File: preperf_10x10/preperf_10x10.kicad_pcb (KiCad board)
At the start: 2 copper layers, 355.3 x 107.6 mm, 1356 parts, among them J1 Conn_01x02_Pin, J2 Conn_01x02_Pin, J3 Conn_01x02_Pin, J4 Conn_01x01_Pin, J5 Conn_01x01_Pin, J6 Conn_01x01_Pin, J7 Conn_01x01_Pin, J8 Conn_01x01_Pin, J9 Conn_01x01_Pin, Q1 BC548, Q2 BC558, SW1 SW_DIP_x06, SW2 SW_Push, U1 LM7805_TO220, U10 74LS14, U2 74LS08, U3 74LS32, U4 74LS04, U5 74LS02, U6 7400, U7 74LS86

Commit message: Update. Delete TP4
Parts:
- removed 2 (x1296): , 
- removed the REF** at (451.5, 55.9)
- removed the REF** at (451.5, 150.5)
- removed the REF** at (356.9, 55.9)
- removed the REF** at (356.9, 150.5)
- RN1: footprint Resistor_THT:R_Array_SIP7 -> Resistor_THT:R_Array_SIP8
- moved D4 2.54 mm to (147.3, 66.0)
- moved D6 2.54 mm to (147.3, 71.1)
- moved D8 2.54 mm to (147.3, 76.2)
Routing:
- net GND: track 385.8 -> 360.4 mm, vias 4 -> 6
- net +5V: track 335.1 -> 330.0 mm, vias 9 -> 11
- net /Logica/E: track 61.0 -> 63.5 mm
- net /Logica/C: track 50.8 -> 53.3 mm
- net /Logica/A: track 12.7 -> 15.2 mm
- net Net-(D8-A): track 7.62 -> 5.08 mm
- net Net-(D6-A): track 7.62 -> 5.08 mm
- net Net-(D4-A): track 7.62 -> 5.08 mm
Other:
- board size 355.3 x 107.6 mm -> 100 x 100 mm

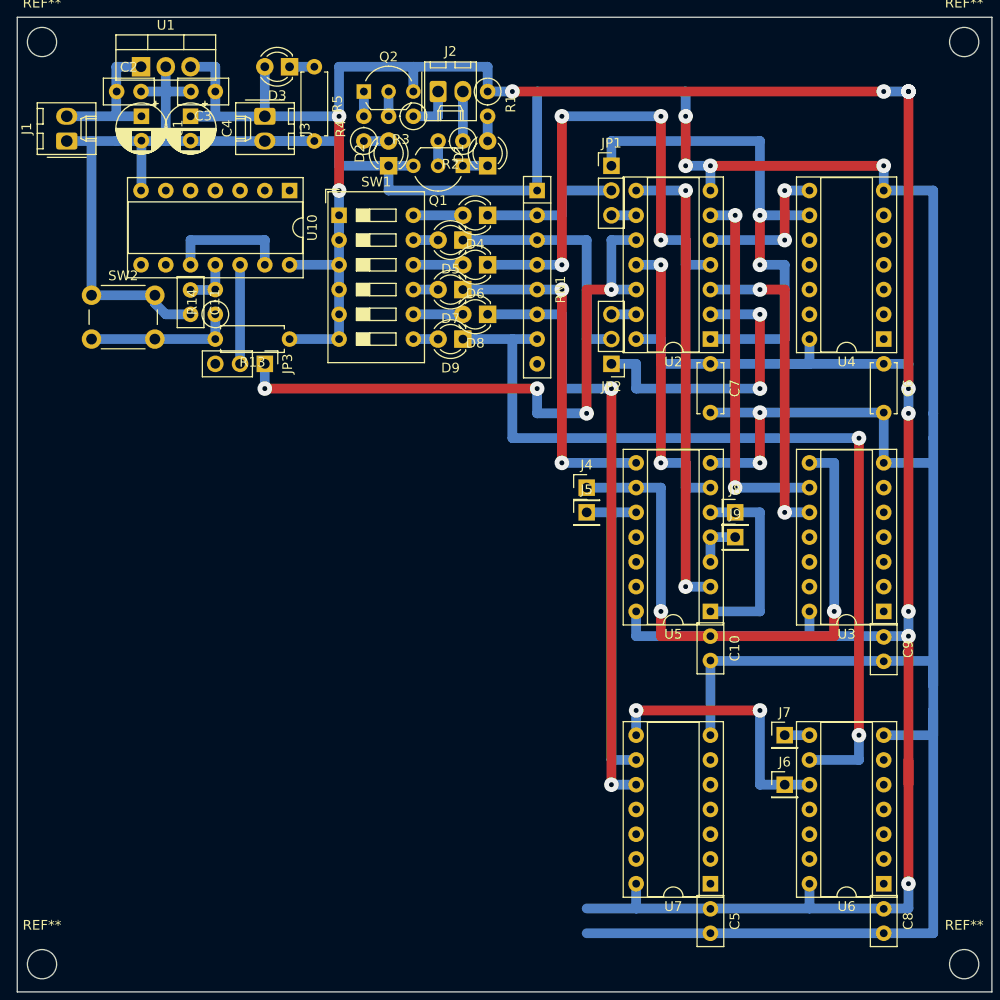
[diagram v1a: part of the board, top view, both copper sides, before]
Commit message: Added BCD Up counter with JK FF
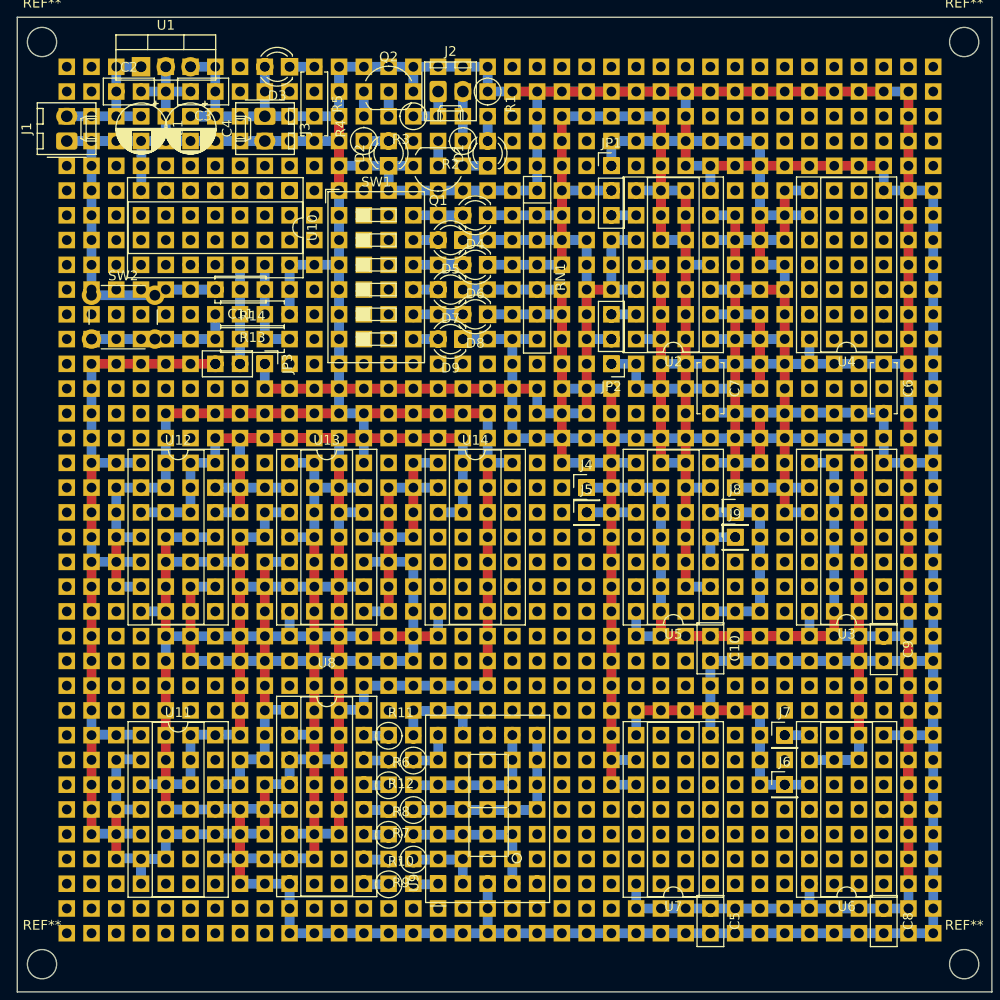
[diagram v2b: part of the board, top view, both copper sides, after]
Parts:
- added 1: , , F.Cu at (106.7, 50.8)
- added 10: , , F.Cu at (129.5, 50.8)
- added 100: , , F.Cu at (175.3, 55.9)
- added 1000: , , F.Cu at (175.3, 119.4)
- added 1001: , , F.Cu at (177.8, 119.4)
- added 1002: , , F.Cu at (180.3, 119.4)
- added 1003: , , F.Cu at (182.9, 119.4)
- added 1004: , , F.Cu at (185.4, 119.4)
- added 1005: , , F.Cu at (188.0, 119.4)
- added 1006: , , F.Cu at (190.5, 119.4)
- added 1007: , , F.Cu at (193.0, 119.4)
- added 1008: , , F.Cu at (104.1, 121.9)
- added 1009: , , F.Cu at (106.7, 121.9)
- added 101: , , F.Cu at (177.8, 55.9)
- added 1010: , , F.Cu at (109.2, 121.9)
- added 1011: , , F.Cu at (111.8, 121.9)
- added 1012: , , F.Cu at (114.3, 121.9)
- added 1013: , , F.Cu at (116.8, 121.9)
- added 1014: , , F.Cu at (119.4, 121.9)
- added 1015: , , F.Cu at (121.9, 121.9)
- added 1016: , , F.Cu at (124.5, 121.9)
- added 1017: , , F.Cu at (127.0, 121.9)
- added 1018: , , F.Cu at (129.5, 121.9)
- added 1019: , , F.Cu at (132.1, 121.9)
- added 102: , , F.Cu at (180.3, 55.9)
- added 1020: , , F.Cu at (134.6, 121.9)
- added 1021: , , F.Cu at (137.2, 121.9)
- added 1022: , , F.Cu at (139.7, 121.9)
- added 1023: , , F.Cu at (142.2, 121.9)
- added 1024: , , F.Cu at (144.8, 121.9)
- added 1025: , , F.Cu at (147.3, 121.9)
- added 1026: , , F.Cu at (149.9, 121.9)
- added 1027: , , F.Cu at (152.4, 121.9)
- added 1028: , , F.Cu at (154.9, 121.9)
- added 1029: , , F.Cu at (157.5, 121.9)
- added 103: , , F.Cu at (182.9, 55.9)
- added 1030: , , F.Cu at (160.0, 121.9)
- added 1031: , , F.Cu at (162.6, 121.9)
- added 1032: , , F.Cu at (165.1, 121.9)
- added 1033: , , F.Cu at (167.6, 121.9)
- added 1034: , , F.Cu at (170.2, 121.9)
- added 1035: , , F.Cu at (172.7, 121.9)
- added 1036: , , F.Cu at (175.3, 121.9)
- added 1037: , , F.Cu at (177.8, 121.9)
- added 1038: , , F.Cu at (180.3, 121.9)
- added 1039: , , F.Cu at (182.9, 121.9)
- added 104: , , F.Cu at (185.4, 55.9)
- added 1040: , , F.Cu at (185.4, 121.9)
- added 1041: , , F.Cu at (188.0, 121.9)
- added 1042: , , F.Cu at (190.5, 121.9)
- added 1043: , , F.Cu at (193.0, 121.9)
- added 1044: , , F.Cu at (104.1, 124.5)
- added 1045: , , F.Cu at (106.7, 124.5)
- added 1046: , , F.Cu at (109.2, 124.5)
- added 1047: , , F.Cu at (111.8, 124.5)
- added 1048: , , F.Cu at (114.3, 124.5)
- added 1049: , , F.Cu at (116.8, 124.5)
- added 105: , , F.Cu at (188.0, 55.9)
- added 1050: , , F.Cu at (119.4, 124.5)
- added 1051: , , F.Cu at (121.9, 124.5)
- added 1052: , , F.Cu at (124.5, 124.5)
- added 1053: , , F.Cu at (127.0, 124.5)
- added 1054: , , F.Cu at (129.5, 124.5)
- added 1055: , , F.Cu at (132.1, 124.5)
- added 1056: , , F.Cu at (134.6, 124.5)
- added 1057: , , F.Cu at (137.2, 124.5)
- added 1058: , , F.Cu at (139.7, 124.5)
- added 1059: , , F.Cu at (142.2, 124.5)
- added 106: , , F.Cu at (190.5, 55.9)
- added 1060: , , F.Cu at (144.8, 124.5)
- added 1061: , , F.Cu at (147.3, 124.5)
- added 1062: , , F.Cu at (149.9, 124.5)
- added 1063: , , F.Cu at (152.4, 124.5)
- added 1064: , , F.Cu at (154.9, 124.5)
- added 1065: , , F.Cu at (157.5, 124.5)
- added 1066: , , F.Cu at (160.0, 124.5)
- added 1067: , , F.Cu at (162.6, 124.5)
- added 1068: , , F.Cu at (165.1, 124.5)
- added 1069: , , F.Cu at (167.6, 124.5)
- added 107: , , F.Cu at (193.0, 55.9)
- added 1070: , , F.Cu at (170.2, 124.5)
- added 1071: , , F.Cu at (172.7, 124.5)
- added 1072: , , F.Cu at (175.3, 124.5)
- added 1073: , , F.Cu at (177.8, 124.5)
- added 1074: , , F.Cu at (180.3, 124.5)
- added 1075: , , F.Cu at (182.9, 124.5)
- added 1076: , , F.Cu at (185.4, 124.5)
- added 1077: , , F.Cu at (188.0, 124.5)
- added 1078: , , F.Cu at (190.5, 124.5)
- added 1079: , , F.Cu at (193.0, 124.5)
- added 108: , , F.Cu at (104.1, 58.4)
- added 1080: , , F.Cu at (104.1, 127.0)
- added 1081: , , F.Cu at (106.7, 127.0)
- added 1082: , , F.Cu at (109.2, 127.0)
- added 1083: , , F.Cu at (111.8, 127.0)
- added 1084: , , F.Cu at (114.3, 127.0)
- added 1085: , , F.Cu at (116.8, 127.0)
- added 1086: , , F.Cu at (119.4, 127.0)
- added 1087: , , F.Cu at (121.9, 127.0)
- added 1088: , , F.Cu at (124.5, 127.0)
- added 1089: , , F.Cu at (127.0, 127.0)
- added 109: , , F.Cu at (106.7, 58.4)
- added 1090: , , F.Cu at (129.5, 127.0)
- added 1091: , , F.Cu at (132.1, 127.0)
- added 1092: , , F.Cu at (134.6, 127.0)
- added 1093: , , F.Cu at (137.2, 127.0)
- added 1094: , , F.Cu at (139.7, 127.0)
- added 1095: , , F.Cu at (142.2, 127.0)
- added 1096: , , F.Cu at (144.8, 127.0)
- added 1097: , , F.Cu at (147.3, 127.0)
- added 1098: , , F.Cu at (149.9, 127.0)
- added 1099: , , F.Cu at (152.4, 127.0)
- added 11: , , F.Cu at (132.1, 50.8)
- added 110: , , F.Cu at (109.2, 58.4)
- added 1100: , , F.Cu at (154.9, 127.0)
- added 1101: , , F.Cu at (157.5, 127.0)
- added 1102: , , F.Cu at (160.0, 127.0)
- added 1103: , , F.Cu at (162.6, 127.0)
- added 1104: , , F.Cu at (165.1, 127.0)
- added 1105: , , F.Cu at (167.6, 127.0)
- added 1106: , , F.Cu at (170.2, 127.0)
- added 1107: , , F.Cu at (172.7, 127.0)
- added 1108: , , F.Cu at (175.3, 127.0)
- added 1109: , , F.Cu at (177.8, 127.0)
- added 111: , , F.Cu at (111.8, 58.4)
- added 1110: , , F.Cu at (180.3, 127.0)
- added 1111: , , F.Cu at (182.9, 127.0)
- added 1112: , , F.Cu at (185.4, 127.0)
- added 1113: , , F.Cu at (188.0, 127.0)
- added 1114: , , F.Cu at (190.5, 127.0)
- added 1115: , , F.Cu at (193.0, 127.0)
- added 1116: , , F.Cu at (104.1, 129.5)
- added 1117: , , F.Cu at (106.7, 129.5)
- added 1118: , , F.Cu at (109.2, 129.5)
- added 1119: , , F.Cu at (111.8, 129.5)
- added 112: , , F.Cu at (114.3, 58.4)
- added 1120: , , F.Cu at (114.3, 129.5)
- added 1121: , , F.Cu at (116.8, 129.5)
- added 1122: , , F.Cu at (119.4, 129.5)
- added 1123: , , F.Cu at (121.9, 129.5)
- added 1124: , , F.Cu at (124.5, 129.5)
- added 1125: , , F.Cu at (127.0, 129.5)
- added 1126: , , F.Cu at (129.5, 129.5)
- added 1127: , , F.Cu at (132.1, 129.5)
- added 1128: , , F.Cu at (134.6, 129.5)
- added 1129: , , F.Cu at (137.2, 129.5)
- added 113: , , F.Cu at (116.8, 58.4)
- added 1130: , , F.Cu at (139.7, 129.5)
- added 1131: , , F.Cu at (142.2, 129.5)
- added 1132: , , F.Cu at (144.8, 129.5)
- added 1133: , , F.Cu at (147.3, 129.5)
- added 1134: , , F.Cu at (149.9, 129.5)
- added 1135: , , F.Cu at (152.4, 129.5)
- added 1136: , , F.Cu at (154.9, 129.5)
- added 1137: , , F.Cu at (157.5, 129.5)
- added 1138: , , F.Cu at (160.0, 129.5)
- added 1139: , , F.Cu at (162.6, 129.5)
- added 114: , , F.Cu at (119.4, 58.4)
- added 1140: , , F.Cu at (165.1, 129.5)
- added 1141: , , F.Cu at (167.6, 129.5)
- added 1142: , , F.Cu at (170.2, 129.5)
- added 1143: , , F.Cu at (172.7, 129.5)
- added 1144: , , F.Cu at (175.3, 129.5)
- added 1145: , , F.Cu at (177.8, 129.5)
- added 1146: , , F.Cu at (180.3, 129.5)
- added 1147: , , F.Cu at (182.9, 129.5)
- added 1148: , , F.Cu at (185.4, 129.5)
- added 1149: , , F.Cu at (188.0, 129.5)
- added 115: , , F.Cu at (121.9, 58.4)
- added 1150: , , F.Cu at (190.5, 129.5)
- added 1151: , , F.Cu at (193.0, 129.5)
- added 1152: , , F.Cu at (104.1, 132.1)
- added 1153: , , F.Cu at (106.7, 132.1)
- added 1154: , , F.Cu at (109.2, 132.1)
- added 1155: , , F.Cu at (111.8, 132.1)
- added 1156: , , F.Cu at (114.3, 132.1)
- added 1157: , , F.Cu at (116.8, 132.1)
- added 1158: , , F.Cu at (119.4, 132.1)
- added 1159: , , F.Cu at (121.9, 132.1)
- added 116: , , F.Cu at (124.5, 58.4)
- added 1160: , , F.Cu at (124.5, 132.1)
- added 1161: , , F.Cu at (127.0, 132.1)
- added 1162: , , F.Cu at (129.5, 132.1)
- added 1163: , , F.Cu at (132.1, 132.1)
- added 1164: , , F.Cu at (134.6, 132.1)
- added 1165: , , F.Cu at (137.2, 132.1)
- added 1166: , , F.Cu at (139.7, 132.1)
- added 1167: , , F.Cu at (142.2, 132.1)
- added 1168: , , F.Cu at (144.8, 132.1)
- added 1169: , , F.Cu at (147.3, 132.1)
- added 117: , , F.Cu at (127.0, 58.4)
- added 1170: , , F.Cu at (149.9, 132.1)
- added 1171: , , F.Cu at (152.4, 132.1)
- added 1172: , , F.Cu at (154.9, 132.1)
- added 1173: , , F.Cu at (157.5, 132.1)
- added 1174: , , F.Cu at (160.0, 132.1)
- added 1175: , , F.Cu at (162.6, 132.1)
- added 1176: , , F.Cu at (165.1, 132.1)
- added 1177: , , F.Cu at (167.6, 132.1)
- added 1178: , , F.Cu at (170.2, 132.1)
- added 1179: , , F.Cu at (172.7, 132.1)
- added 118: , , F.Cu at (129.5, 58.4)
- added 1180: , , F.Cu at (175.3, 132.1)
- added 1181: , , F.Cu at (177.8, 132.1)
- added 1182: , , F.Cu at (180.3, 132.1)
- added 1183: , , F.Cu at (182.9, 132.1)
- added 1184: , , F.Cu at (185.4, 132.1)
- added 1185: , , F.Cu at (188.0, 132.1)
- added 1186: , , F.Cu at (190.5, 132.1)
- added 1187: , , F.Cu at (193.0, 132.1)
- added 1188: , , F.Cu at (104.1, 134.6)
- added 1189: , , F.Cu at (106.7, 134.6)
- added 119: , , F.Cu at (132.1, 58.4)
- added 1190: , , F.Cu at (109.2, 134.6)
- added 1191: , , F.Cu at (111.8, 134.6)
- added 1192: , , F.Cu at (114.3, 134.6)
- added 1193: , , F.Cu at (116.8, 134.6)
- added 1194: , , F.Cu at (119.4, 134.6)
- added 1195: , , F.Cu at (121.9, 134.6)
- added 1196: , , F.Cu at (124.5, 134.6)
- added 1197: , , F.Cu at (127.0, 134.6)
- added 1198: , , F.Cu at (129.5, 134.6)
- added 1199: , , F.Cu at (132.1, 134.6)
- added 12: , , F.Cu at (134.6, 50.8)
- added 120: , , F.Cu at (134.6, 58.4)
- added 1200: , , F.Cu at (134.6, 134.6)
- added 1201: , , F.Cu at (137.2, 134.6)
- added 1202: , , F.Cu at (139.7, 134.6)
- added 1203: , , F.Cu at (142.2, 134.6)
- added 1204: , , F.Cu at (144.8, 134.6)
- added 1205: , , F.Cu at (147.3, 134.6)
- added 1206: , , F.Cu at (149.9, 134.6)
- added 1207: , , F.Cu at (152.4, 134.6)
- added 1208: , , F.Cu at (154.9, 134.6)
- added 1209: , , F.Cu at (157.5, 134.6)
- added 121: , , F.Cu at (137.2, 58.4)
- added 1210: , , F.Cu at (160.0, 134.6)
- added 1211: , , F.Cu at (162.6, 134.6)
- added 1212: , , F.Cu at (165.1, 134.6)
- added 1213: , , F.Cu at (167.6, 134.6)
- added 1214: , , F.Cu at (170.2, 134.6)
- added 1215: , , F.Cu at (172.7, 134.6)
- added 1216: , , F.Cu at (175.3, 134.6)
- added 1217: , , F.Cu at (177.8, 134.6)
- added 1218: , , F.Cu at (180.3, 134.6)
- added 1219: , , F.Cu at (182.9, 134.6)
- added 122: , , F.Cu at (139.7, 58.4)
- added 1220: , , F.Cu at (185.4, 134.6)
- added 1221: , , F.Cu at (188.0, 134.6)
- added 1222: , , F.Cu at (190.5, 134.6)
- added 1223: , , F.Cu at (193.0, 134.6)
- added 1224: , , F.Cu at (104.1, 137.2)
- added 1225: , , F.Cu at (106.7, 137.2)
- added 1226: , , F.Cu at (109.2, 137.2)
- added 1227: , , F.Cu at (111.8, 137.2)
- added 1228: , , F.Cu at (114.3, 137.2)
- added 1229: , , F.Cu at (116.8, 137.2)
- added 123: , , F.Cu at (142.2, 58.4)
- added 1230: , , F.Cu at (119.4, 137.2)
- added 1231: , , F.Cu at (121.9, 137.2)
- added 1232: , , F.Cu at (124.5, 137.2)
- added 1233: , , F.Cu at (127.0, 137.2)
- added 1234: , , F.Cu at (129.5, 137.2)
- added 1235: , , F.Cu at (132.1, 137.2)
- added 1236: , , F.Cu at (134.6, 137.2)
- added 1237: , , F.Cu at (137.2, 137.2)
- added 1238: , , F.Cu at (139.7, 137.2)
- added 1239: , , F.Cu at (142.2, 137.2)
- added 124: , , F.Cu at (144.8, 58.4)
- added 1240: , , F.Cu at (144.8, 137.2)
- added 1241: , , F.Cu at (147.3, 137.2)
- added 1242: , , F.Cu at (149.9, 137.2)
- added 1243: , , F.Cu at (152.4, 137.2)
- added 1244: , , F.Cu at (154.9, 137.2)
- added 1245: , , F.Cu at (157.5, 137.2)
- added 1246: , , F.Cu at (160.0, 137.2)
- added 1247: , , F.Cu at (162.6, 137.2)
- added 1248: , , F.Cu at (165.1, 137.2)
- added 1249: , , F.Cu at (167.6, 137.2)
- added 125: , , F.Cu at (147.3, 58.4)
- added 1250: , , F.Cu at (170.2, 137.2)
- added 1251: , , F.Cu at (172.7, 137.2)
- added 1252: , , F.Cu at (175.3, 137.2)
- added 1253: , , F.Cu at (177.8, 137.2)
- added 1254: , , F.Cu at (180.3, 137.2)
- added 1255: , , F.Cu at (182.9, 137.2)
- added 1256: , , F.Cu at (185.4, 137.2)
- added 1257: , , F.Cu at (188.0, 137.2)
- added 1258: , , F.Cu at (190.5, 137.2)
- added 1259: , , F.Cu at (193.0, 137.2)
- added 126: , , F.Cu at (149.9, 58.4)
- added 1260: , , F.Cu at (104.1, 139.7)
- added 1261: , , F.Cu at (106.7, 139.7)
- added 1262: , , F.Cu at (109.2, 139.7)
- added 1263: , , F.Cu at (111.8, 139.7)
- added 1264: , , F.Cu at (114.3, 139.7)
- added 1265: , , F.Cu at (116.8, 139.7)
- added 1266: , , F.Cu at (119.4, 139.7)
- added 1267: , , F.Cu at (121.9, 139.7)
- added 1268: , , F.Cu at (124.5, 139.7)
- added 1269: , , F.Cu at (127.0, 139.7)
- added 127: , , F.Cu at (152.4, 58.4)
- added 1270: , , F.Cu at (129.5, 139.7)
- added 1271: , , F.Cu at (132.1, 139.7)
- added 1272: , , F.Cu at (134.6, 139.7)
- added 1273: , , F.Cu at (137.2, 139.7)
- added 1274: , , F.Cu at (139.7, 139.7)
- added 1275: , , F.Cu at (142.2, 139.7)
- added 1276: , , F.Cu at (144.8, 139.7)
- added 1277: , , F.Cu at (147.3, 139.7)
- added 1278: , , F.Cu at (149.9, 139.7)
- added 1279: , , F.Cu at (152.4, 139.7)
- added 128: , , F.Cu at (154.9, 58.4)
- added 1280: , , F.Cu at (154.9, 139.7)
- added 1281: , , F.Cu at (157.5, 139.7)
- added 1282: , , F.Cu at (160.0, 139.7)
- added 1283: , , F.Cu at (162.6, 139.7)
- added 1284: , , F.Cu at (165.1, 139.7)
- added 1285: , , F.Cu at (167.6, 139.7)
- added 1286: , , F.Cu at (170.2, 139.7)
- added 1287: , , F.Cu at (172.7, 139.7)
- added 1288: , , F.Cu at (175.3, 139.7)
- added 1289: , , F.Cu at (177.8, 139.7)
- added 129: , , F.Cu at (157.5, 58.4)
- added 1290: , , F.Cu at (180.3, 139.7)
- added 1291: , , F.Cu at (182.9, 139.7)
- added 1292: , , F.Cu at (185.4, 139.7)
- added 1293: , , F.Cu at (188.0, 139.7)
- added 1294: , , F.Cu at (190.5, 139.7)
- added 1295: , , F.Cu at (193.0, 139.7)
- added 13: , , F.Cu at (137.2, 50.8)
- added 130: , , F.Cu at (160.0, 58.4)
- added 131: , , F.Cu at (162.6, 58.4)
- added 132: , , F.Cu at (165.1, 58.4)
- added 133: , , F.Cu at (167.6, 58.4)
- added 134: , , F.Cu at (170.2, 58.4)
- added 135: , , F.Cu at (172.7, 58.4)
- added 136: , , F.Cu at (175.3, 58.4)
- added 137: , , F.Cu at (177.8, 58.4)
- added 138: , , F.Cu at (180.3, 58.4)
- added 139: , , F.Cu at (182.9, 58.4)
- added 14: , , F.Cu at (139.7, 50.8)
- added 140: , , F.Cu at (185.4, 58.4)
- added 141: , , F.Cu at (188.0, 58.4)
- added 142: , , F.Cu at (190.5, 58.4)
- added 143: , , F.Cu at (193.0, 58.4)
- added 144: , , F.Cu at (104.1, 61.0)
- added 145: , , F.Cu at (106.7, 61.0)
- added 146: , , F.Cu at (109.2, 61.0)
- added 147: , , F.Cu at (111.8, 61.0)
- added 148: , , F.Cu at (114.3, 61.0)
- added 149: , , F.Cu at (116.8, 61.0)
- added 15: , , F.Cu at (142.2, 50.8)
- added 150: , , F.Cu at (119.4, 61.0)
- added 151: , , F.Cu at (121.9, 61.0)
- added 152: , , F.Cu at (124.5, 61.0)
- added 153: , , F.Cu at (127.0, 61.0)
- added 154: , , F.Cu at (129.5, 61.0)
- added 155: , , F.Cu at (132.1, 61.0)
- added 156: , , F.Cu at (134.6, 61.0)
- added 157: , , F.Cu at (137.2, 61.0)
- added 158: , , F.Cu at (139.7, 61.0)
- added 159: , , F.Cu at (142.2, 61.0)
- added 16: , , F.Cu at (144.8, 50.8)
- added 160: , , F.Cu at (144.8, 61.0)
- added 161: , , F.Cu at (147.3, 61.0)
- added 162: , , F.Cu at (149.9, 61.0)
- added 163: , , F.Cu at (152.4, 61.0)
- added 164: , , F.Cu at (154.9, 61.0)
- added 165: , , F.Cu at (157.5, 61.0)
- added 166: , , F.Cu at (160.0, 61.0)
- added 167: , , F.Cu at (162.6, 61.0)
- added 168: , , F.Cu at (165.1, 61.0)
- added 169: , , F.Cu at (167.6, 61.0)
- added 17: , , F.Cu at (147.3, 50.8)
- added 170: , , F.Cu at (170.2, 61.0)
- added 171: , , F.Cu at (172.7, 61.0)
- added 172: , , F.Cu at (175.3, 61.0)
- added 173: , , F.Cu at (177.8, 61.0)
- added 174: , , F.Cu at (180.3, 61.0)
- added 175: , , F.Cu at (182.9, 61.0)
- added 176: , , F.Cu at (185.4, 61.0)
- added 177: , , F.Cu at (188.0, 61.0)
- added 178: , , F.Cu at (190.5, 61.0)
- added 179: , , F.Cu at (193.0, 61.0)
- added 18: , , F.Cu at (149.9, 50.8)
- added 180: , , F.Cu at (104.1, 63.5)
- added 181: , , F.Cu at (106.7, 63.5)
- added 182: , , F.Cu at (109.2, 63.5)
- added 183: , , F.Cu at (111.8, 63.5)
- added 184: , , F.Cu at (114.3, 63.5)
- added 185: , , F.Cu at (116.8, 63.5)
- added 186: , , F.Cu at (119.4, 63.5)
- added 187: , , F.Cu at (121.9, 63.5)
- added 188: , , F.Cu at (124.5, 63.5)
- added 189: , , F.Cu at (127.0, 63.5)
- added 19: , , F.Cu at (152.4, 50.8)
- added 190: , , F.Cu at (129.5, 63.5)
- added 191: , , F.Cu at (132.1, 63.5)
- added 193: , , F.Cu at (137.2, 63.5)
- added 195: , , F.Cu at (142.2, 63.5)
- added 196: , , F.Cu at (144.8, 63.5)
- added 197: , , F.Cu at (147.3, 63.5)
- added 198: , , F.Cu at (149.9, 63.5)
- added 199: , , F.Cu at (152.4, 63.5)
- added 2: , , F.Cu at (109.2, 50.8)
- added 20: , , F.Cu at (154.9, 50.8)
- added 200: , , F.Cu at (154.9, 63.5)
- added 201: , , F.Cu at (157.5, 63.5)
- added 202: , , F.Cu at (160.0, 63.5)
- added 203: , , F.Cu at (162.6, 63.5)
- added 204: , , F.Cu at (165.1, 63.5)
- added 205: , , F.Cu at (167.6, 63.5)
- added 206: , , F.Cu at (170.2, 63.5)
- added 207: , , F.Cu at (172.7, 63.5)
- added 208: , , F.Cu at (175.3, 63.5)
- added 209: , , F.Cu at (177.8, 63.5)
- added 21: , , F.Cu at (157.5, 50.8)
- added 210: , , F.Cu at (180.3, 63.5)
- added 211: , , F.Cu at (182.9, 63.5)
- added 212: , , F.Cu at (185.4, 63.5)
- added 213: , , F.Cu at (188.0, 63.5)
- added 214: , , F.Cu at (190.5, 63.5)
- added 215: , , F.Cu at (193.0, 63.5)
- added 216: , , F.Cu at (104.1, 66.0)
- added 217: , , F.Cu at (106.7, 66.0)
- added 218: , , F.Cu at (109.2, 66.0)
- added 219: , , F.Cu at (111.8, 66.0)
- added 22: , , F.Cu at (160.0, 50.8)
- added 220: , , F.Cu at (114.3, 66.0)
- added 221: , , F.Cu at (116.8, 66.0)
- added 222: , , F.Cu at (119.4, 66.0)
- added 223: , , F.Cu at (121.9, 66.0)
- added 224: , , F.Cu at (124.5, 66.0)
- added 225: , , F.Cu at (127.0, 66.0)
- added 226: , , F.Cu at (129.5, 66.0)
- added 227: , , F.Cu at (132.1, 66.0)
- added 228: , , F.Cu at (134.6, 66.0)
- added 229: , , F.Cu at (137.2, 66.0)
- added 23: , , F.Cu at (162.6, 50.8)
- added 230: , , F.Cu at (139.7, 66.0)
- added 231: , , F.Cu at (142.2, 66.0)
- added 232: , , F.Cu at (144.8, 66.0)
- added 233: , , F.Cu at (147.3, 66.0)
- added 234: , , F.Cu at (149.9, 66.0)
- added 235: , , F.Cu at (152.4, 66.0)
- added 236: , , F.Cu at (154.9, 66.0)
- added 237: , , F.Cu at (157.5, 66.0)
- added 238: , , F.Cu at (160.0, 66.0)
- added 239: , , F.Cu at (162.6, 66.0)
- added 24: , , F.Cu at (165.1, 50.8)
- added 240: , , F.Cu at (165.1, 66.0)
- added 241: , , F.Cu at (167.6, 66.0)
- added 242: , , F.Cu at (170.2, 66.0)
- added 243: , , F.Cu at (172.7, 66.0)
- added 244: , , F.Cu at (175.3, 66.0)
- added 245: , , F.Cu at (177.8, 66.0)
- added 246: , , F.Cu at (180.3, 66.0)
- added 247: , , F.Cu at (182.9, 66.0)
- added 248: , , F.Cu at (185.4, 66.0)
- added 249: , , F.Cu at (188.0, 66.0)
- added 25: , , F.Cu at (167.6, 50.8)
- added 250: , , F.Cu at (190.5, 66.0)
- added 251: , , F.Cu at (193.0, 66.0)
- added 252: , , F.Cu at (104.1, 68.6)
- added 253: , , F.Cu at (106.7, 68.6)
- added 254: , , F.Cu at (109.2, 68.6)
- added 255: , , F.Cu at (111.8, 68.6)
- added 256: , , F.Cu at (114.3, 68.6)
- added 257: , , F.Cu at (116.8, 68.6)
- added 258: , , F.Cu at (119.4, 68.6)
- added 259: , , F.Cu at (121.9, 68.6)
- added 26: , , F.Cu at (170.2, 50.8)
- added 260: , , F.Cu at (124.5, 68.6)
- added 261: , , F.Cu at (127.0, 68.6)
- added 262: , , F.Cu at (129.5, 68.6)
- added 263: , , F.Cu at (132.1, 68.6)
- added 264: , , F.Cu at (134.6, 68.6)
- added 265: , , F.Cu at (137.2, 68.6)
- added 266: , , F.Cu at (139.7, 68.6)
- added 267: , , F.Cu at (142.2, 68.6)
- added 268: , , F.Cu at (144.8, 68.6)
- added 269: , , F.Cu at (147.3, 68.6)
- added 27: , , F.Cu at (172.7, 50.8)
- added 270: , , F.Cu at (149.9, 68.6)
- added 271: , , F.Cu at (152.4, 68.6)
- added 272: , , F.Cu at (154.9, 68.6)
- added 273: , , F.Cu at (157.5, 68.6)
- added 274: , , F.Cu at (160.0, 68.6)
- added 275: , , F.Cu at (162.6, 68.6)
- added 276: , , F.Cu at (165.1, 68.6)
- added 277: , , F.Cu at (167.6, 68.6)
- added 278: , , F.Cu at (170.2, 68.6)
- added 279: , , F.Cu at (172.7, 68.6)
- added 28: , , F.Cu at (175.3, 50.8)
- added 280: , , F.Cu at (175.3, 68.6)
- added 281: , , F.Cu at (177.8, 68.6)
- added 282: , , F.Cu at (180.3, 68.6)
- added 283: , , F.Cu at (182.9, 68.6)
- added 284: , , F.Cu at (185.4, 68.6)
- added 285: , , F.Cu at (188.0, 68.6)
- added 286: , , F.Cu at (190.5, 68.6)
- added 287: , , F.Cu at (193.0, 68.6)
- added 288: , , F.Cu at (104.1, 71.1)
- added 289: , , F.Cu at (106.7, 71.1)
- added 29: , , F.Cu at (177.8, 50.8)
- added 290: , , F.Cu at (109.2, 71.1)
- added 291: , , F.Cu at (111.8, 71.1)
- added 292: , , F.Cu at (114.3, 71.1)
- added 293: , , F.Cu at (116.8, 71.1)
- added 294: , , F.Cu at (119.4, 71.1)
- added 295: , , F.Cu at (121.9, 71.1)
- added 296: , , F.Cu at (124.5, 71.1)
- added 297: , , F.Cu at (127.0, 71.1)
- added 298: , , F.Cu at (129.5, 71.1)
- added 299: , , F.Cu at (132.1, 71.1)
- added 3: , , F.Cu at (111.8, 50.8)
- added 30: , , F.Cu at (180.3, 50.8)
- added 300: , , F.Cu at (134.6, 71.1)
- added 301: , , F.Cu at (137.2, 71.1)
- added 302: , , F.Cu at (139.7, 71.1)
- added 303: , , F.Cu at (142.2, 71.1)
- added 304: , , F.Cu at (144.8, 71.1)
- added 305: , , F.Cu at (147.3, 71.1)
- added 306: , , F.Cu at (149.9, 71.1)
- added 307: , , F.Cu at (152.4, 71.1)
- added 308: , , F.Cu at (154.9, 71.1)
- added 309: , , F.Cu at (157.5, 71.1)
- added 31: , , F.Cu at (182.9, 50.8)
- added 310: , , F.Cu at (160.0, 71.1)
- added 311: , , F.Cu at (162.6, 71.1)
- added 312: , , F.Cu at (165.1, 71.1)
- added 313: , , F.Cu at (167.6, 71.1)
- added 314: , , F.Cu at (170.2, 71.1)
- added 315: , , F.Cu at (172.7, 71.1)
- added 316: , , F.Cu at (175.3, 71.1)
- added 317: , , F.Cu at (177.8, 71.1)
- added 318: , , F.Cu at (180.3, 71.1)
- added 319: , , F.Cu at (182.9, 71.1)
- added 32: , , F.Cu at (185.4, 50.8)
- added 320: , , F.Cu at (185.4, 71.1)
- added 321: , , F.Cu at (188.0, 71.1)
- added 322: , , F.Cu at (190.5, 71.1)
- added 323: , , F.Cu at (193.0, 71.1)
- added 324: , , F.Cu at (104.1, 73.7)
- added 325: , , F.Cu at (106.7, 73.7)
- added 326: , , F.Cu at (109.2, 73.7)
- added 327: , , F.Cu at (111.8, 73.7)
- added 328: , , F.Cu at (114.3, 73.7)
- added 329: , , F.Cu at (116.8, 73.7)
- added 33: , , F.Cu at (188.0, 50.8)
- added 330: , , F.Cu at (119.4, 73.7)
- added 331: , , F.Cu at (121.9, 73.7)
- added 332: , , F.Cu at (124.5, 73.7)
- added 333: , , F.Cu at (127.0, 73.7)
- added 334: , , F.Cu at (129.5, 73.7)
- added 335: , , F.Cu at (132.1, 73.7)
- added 336: , , F.Cu at (134.6, 73.7)
- added 337: , , F.Cu at (137.2, 73.7)
- added 338: , , F.Cu at (139.7, 73.7)
- added 339: , , F.Cu at (142.2, 73.7)
- added 34: , , F.Cu at (190.5, 50.8)
- added 340: , , F.Cu at (144.8, 73.7)
- added 341: , , F.Cu at (147.3, 73.7)
- added 342: , , F.Cu at (149.9, 73.7)
- added 343: , , F.Cu at (152.4, 73.7)
- added 344: , , F.Cu at (154.9, 73.7)
- added 345: , , F.Cu at (157.5, 73.7)
- added 346: , , F.Cu at (160.0, 73.7)
- added 347: , , F.Cu at (162.6, 73.7)
- added 348: , , F.Cu at (165.1, 73.7)
- added 349: , , F.Cu at (167.6, 73.7)
- added 35: , , F.Cu at (193.0, 50.8)
- added 350: , , F.Cu at (170.2, 73.7)
- added 351: , , F.Cu at (172.7, 73.7)
- added 352: , , F.Cu at (175.3, 73.7)
- added 353: , , F.Cu at (177.8, 73.7)
- added 354: , , F.Cu at (180.3, 73.7)
- added 355: , , F.Cu at (182.9, 73.7)
- added 356: , , F.Cu at (185.4, 73.7)
- added 357: , , F.Cu at (188.0, 73.7)
- added 358: , , F.Cu at (190.5, 73.7)
- added 359: , , F.Cu at (193.0, 73.7)
- added 36: , , F.Cu at (104.1, 53.3)
- added 360: , , F.Cu at (104.1, 76.2)
- added 361: , , F.Cu at (106.7, 76.2)
- added 362: , , F.Cu at (109.2, 76.2)
- added 363: , , F.Cu at (111.8, 76.2)
- added 364: , , F.Cu at (114.3, 76.2)
- added 365: , , F.Cu at (116.8, 76.2)
- added 366: , , F.Cu at (119.4, 76.2)
- added 367: , , F.Cu at (121.9, 76.2)
- added 368: , , F.Cu at (124.5, 76.2)
- added 369: , , F.Cu at (127.0, 76.2)
- added 37: , , F.Cu at (106.7, 53.3)
- added 370: , , F.Cu at (129.5, 76.2)
- added 371: , , F.Cu at (132.1, 76.2)
- added 372: , , F.Cu at (134.6, 76.2)
- added 373: , , F.Cu at (137.2, 76.2)
- added 374: , , F.Cu at (139.7, 76.2)
- added 375: , , F.Cu at (142.2, 76.2)
- added 376: , , F.Cu at (144.8, 76.2)
- added 377: , , F.Cu at (147.3, 76.2)
- added 378: , , F.Cu at (149.9, 76.2)
- added 379: , , F.Cu at (152.4, 76.2)
- added 38: , , F.Cu at (109.2, 53.3)
- added 380: , , F.Cu at (154.9, 76.2)
- added 381: , , F.Cu at (157.5, 76.2)
- added 382: , , F.Cu at (160.0, 76.2)
- added 383: , , F.Cu at (162.6, 76.2)
- added 384: , , F.Cu at (165.1, 76.2)
- added 385: , , F.Cu at (167.6, 76.2)
- added 386: , , F.Cu at (170.2, 76.2)
- added 387: , , F.Cu at (172.7, 76.2)
- added 388: , , F.Cu at (175.3, 76.2)
- added 389: , , F.Cu at (177.8, 76.2)
- added 39: , , F.Cu at (111.8, 53.3)
- added 390: , , F.Cu at (180.3, 76.2)
- added 391: , , F.Cu at (182.9, 76.2)
- added 392: , , F.Cu at (185.4, 76.2)
- added 393: , , F.Cu at (188.0, 76.2)
- added 394: , , F.Cu at (190.5, 76.2)
- added 395: , , F.Cu at (193.0, 76.2)
- added 396: , , F.Cu at (104.1, 78.7)
- added 397: , , F.Cu at (106.7, 78.7)
- added 398: , , F.Cu at (109.2, 78.7)
- added 399: , , F.Cu at (111.8, 78.7)
- added 4: , , F.Cu at (114.3, 50.8)
- added 40: , , F.Cu at (114.3, 53.3)
- added 400: , , F.Cu at (114.3, 78.7)
- added 401: , , F.Cu at (116.8, 78.7)
- added 402: , , F.Cu at (119.4, 78.7)
- added 403: , , F.Cu at (121.9, 78.7)
- added 404: , , F.Cu at (124.5, 78.7)
- added 405: , , F.Cu at (127.0, 78.7)
- added 406: , , F.Cu at (129.5, 78.7)
- added 407: , , F.Cu at (132.1, 78.7)
- added 408: , , F.Cu at (134.6, 78.7)
- added 409: , , F.Cu at (137.2, 78.7)
- added 41: , , F.Cu at (116.8, 53.3)
- added 410: , , F.Cu at (139.7, 78.7)
- added 411: , , F.Cu at (142.2, 78.7)
- added 412: , , F.Cu at (144.8, 78.7)
- added 413: , , F.Cu at (147.3, 78.7)
- added 414: , , F.Cu at (149.9, 78.7)
- added 415: , , F.Cu at (152.4, 78.7)
- added 416: , , F.Cu at (154.9, 78.7)
- added 417: , , F.Cu at (157.5, 78.7)
- added 418: , , F.Cu at (160.0, 78.7)
- added 419: , , F.Cu at (162.6, 78.7)
- added 42: , , F.Cu at (119.4, 53.3)
- added 420: , , F.Cu at (165.1, 78.7)
- added 421: , , F.Cu at (167.6, 78.7)
- added 422: , , F.Cu at (170.2, 78.7)
- added 423: , , F.Cu at (172.7, 78.7)
- added 424: , , F.Cu at (175.3, 78.7)
- added 425: , , F.Cu at (177.8, 78.7)
- added 426: , , F.Cu at (180.3, 78.7)
- added 427: , , F.Cu at (182.9, 78.7)
- added 428: , , F.Cu at (185.4, 78.7)
- added 429: , , F.Cu at (188.0, 78.7)
- added 43: , , F.Cu at (121.9, 53.3)
- added 430: , , F.Cu at (190.5, 78.7)
- added 431: , , F.Cu at (193.0, 78.7)
- added 432: , , F.Cu at (104.1, 81.3)
- added 433: , , F.Cu at (106.7, 81.3)
- added 434: , , F.Cu at (109.2, 81.3)
- added 435: , , F.Cu at (111.8, 81.3)
- added 436: , , F.Cu at (114.3, 81.3)
- added 437: , , F.Cu at (116.8, 81.3)
- added 438: , , F.Cu at (119.4, 81.3)
- added 439: , , F.Cu at (121.9, 81.3)
- added 44: , , F.Cu at (124.5, 53.3)
- added 440: , , F.Cu at (124.5, 81.3)
- added 441: , , F.Cu at (127.0, 81.3)
- added 442: , , F.Cu at (129.5, 81.3)
- added 443: , , F.Cu at (132.1, 81.3)
- added 444: , , F.Cu at (134.6, 81.3)
- added 445: , , F.Cu at (137.2, 81.3)
- added 446: , , F.Cu at (139.7, 81.3)
- added 447: , , F.Cu at (142.2, 81.3)
- added 448: , , F.Cu at (144.8, 81.3)
- added 449: , , F.Cu at (147.3, 81.3)
- added 45: , , F.Cu at (127.0, 53.3)
- added 450: , , F.Cu at (149.9, 81.3)
- added 451: , , F.Cu at (152.4, 81.3)
- added 453: , , F.Cu at (157.5, 81.3)
- added 454: , , F.Cu at (160.0, 81.3)
- added 455: , , F.Cu at (162.6, 81.3)
- added 456: , , F.Cu at (165.1, 81.3)
- added 457: , , F.Cu at (167.6, 81.3)
- added 458: , , F.Cu at (170.2, 81.3)
- added 459: , , F.Cu at (172.7, 81.3)
- added 46: , , F.Cu at (129.5, 53.3)
- added 460: , , F.Cu at (175.3, 81.3)
- added 461: , , F.Cu at (177.8, 81.3)
- added 462: , , F.Cu at (180.3, 81.3)
- added 463: , , F.Cu at (182.9, 81.3)
- added 464: , , F.Cu at (185.4, 81.3)
- added 465: , , F.Cu at (188.0, 81.3)
- added 466: , , F.Cu at (190.5, 81.3)
- added 467: , , F.Cu at (193.0, 81.3)
- added 468: , , F.Cu at (104.1, 83.8)
- added 469: , , F.Cu at (106.7, 83.8)
- added 47: , , F.Cu at (132.1, 53.3)
- added 470: , , F.Cu at (109.2, 83.8)
- added 471: , , F.Cu at (111.8, 83.8)
- added 472: , , F.Cu at (114.3, 83.8)
- added 473: , , F.Cu at (116.8, 83.8)
- added 474: , , F.Cu at (119.4, 83.8)
- added 475: , , F.Cu at (121.9, 83.8)
- added 476: , , F.Cu at (124.5, 83.8)
- added 477: , , F.Cu at (127.0, 83.8)
- added 478: , , F.Cu at (129.5, 83.8)
- added 479: , , F.Cu at (132.1, 83.8)
- added 48: , , F.Cu at (134.6, 53.3)
- added 480: , , F.Cu at (134.6, 83.8)
- added 481: , , F.Cu at (137.2, 83.8)
- added 482: , , F.Cu at (139.7, 83.8)
- added 483: , , F.Cu at (142.2, 83.8)
- added 484: , , F.Cu at (144.8, 83.8)
- added 485: , , F.Cu at (147.3, 83.8)
- added 486: , , F.Cu at (149.9, 83.8)
- added 487: , , F.Cu at (152.4, 83.8)
- added 488: , , F.Cu at (154.9, 83.8)
- added 489: , , F.Cu at (157.5, 83.8)
- added 49: , , F.Cu at (137.2, 53.3)
- added 490: , , F.Cu at (160.0, 83.8)
- added 491: , , F.Cu at (162.6, 83.8)
- added 492: , , F.Cu at (165.1, 83.8)
- added 493: , , F.Cu at (167.6, 83.8)
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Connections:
- JP3 pad 3: unconnected-(JP3-B-Pad3) -> /Contador BCD UP/CLK
- U10 pad 10: Net-(U10-Pad10) -> (no net)
- U10 pad 11: Net-(C11-Pad1) -> (no net)
- U10 pad 13: Net-(U10-Pad10) -> Net-(C11-Pad1)
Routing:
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
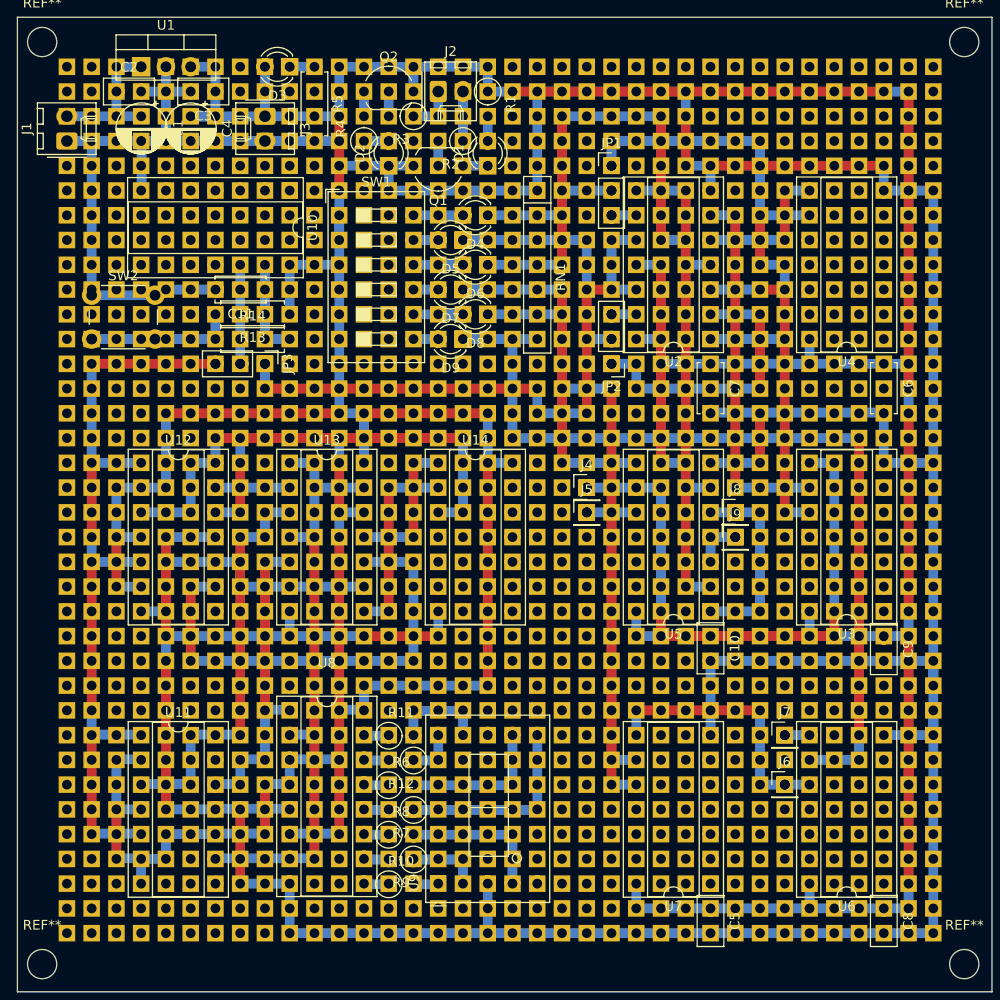
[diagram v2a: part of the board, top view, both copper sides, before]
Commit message: Added BCD Counter UP (FF JK based)  and Power-On-Reset
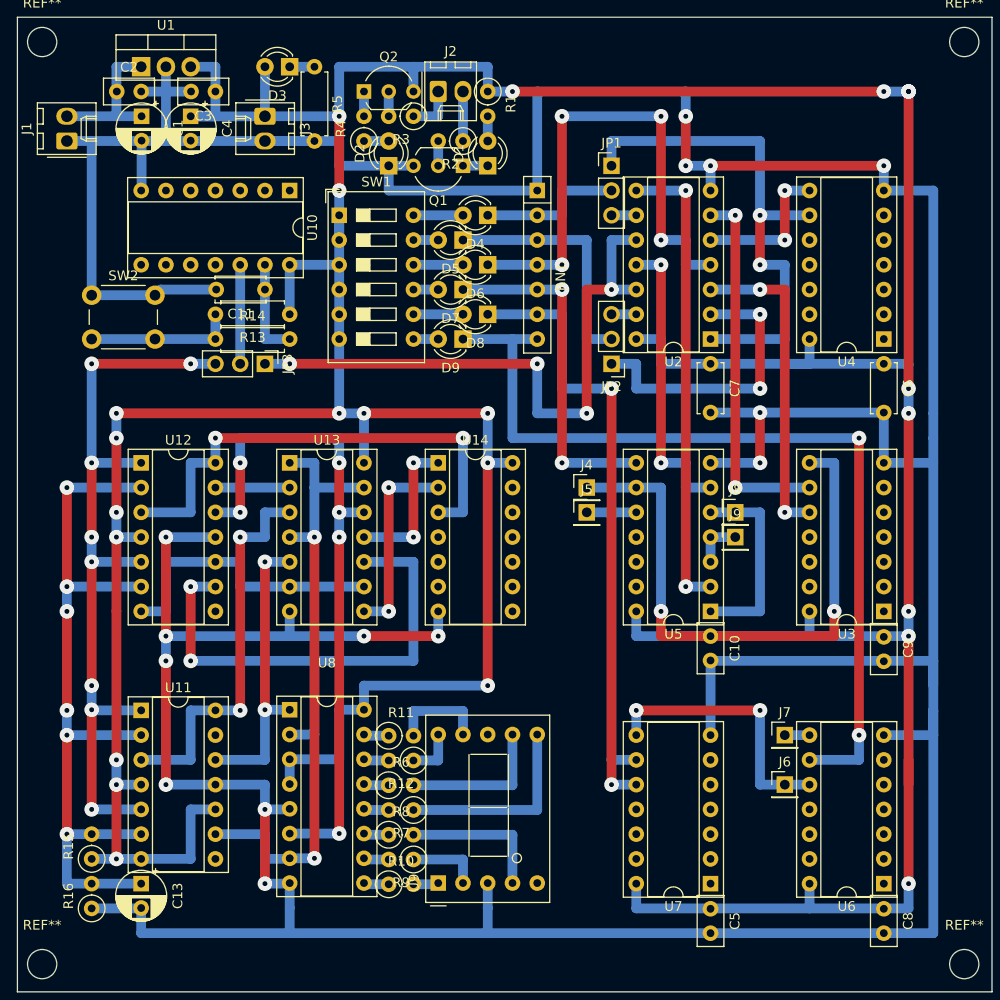
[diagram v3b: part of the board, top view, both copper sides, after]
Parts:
- removed 1, 10, 100, 1000, 1001, 1002, 1003, 1004, 1005, 1006, 1007, 1008, 1009, 101, 1010, 1011, 1012, 1013, 1014, 1015, 1016, 1017, 1018, 1019, 102, 1020, 1021, 1022, 1023, 1024, 1025, 1026, 1027, 1028, 1029, 103, 1030, 1031, 1032, 1033, 1034, 1035, 1036, 1037, 1038, 1039, 104, 1040, 1041, 1042, 1043, 1044, 1045, 1046, 1047, 1048, 1049, 105, 1050, 1051, 1052, 1053, 1054, 1055, 1056, 1057, 1058, 1059, 106, 1060, 1061, 1062, 1063, 1064, 1065, 1066, 1067, 1068, 1069, 107, 1070, 1071, 1072, 1073, 1074, 1075, 1076, 1077, 1078, 1079, 108, 1080, 1081, 1082, 1083, 1084, 1085, 1086, 1087, 1088, 1089, 109, 1090, 1091, 1092, 1093, 1094, 1095, 1096, 1097, 1098, 1099, 11, 110, 1100, 1101, 1102, 1103, 1104, 1105, 1106, 1107, 1108, 1109, 111, 1110, 1111, 1112, 1113, 1114, 1115, 1116, 1117, 1118, 1119, 112, 1120, 1121, 1122, 1123, 1124, 1125, 1126, 1127, 1128, 1129, 113, 1130, 1131, 1132, 1133, 1134, 1135, 1136, 1137, 1138, 1139, 114, 1140, 1141, 1142, 1143, 1144, 1145, 1146, 1147, 1148, 1149, 115, 1150, 1151, 1152, 1153, 1154, 1155, 1156, 1157, 1158, 1159, 116, 1160, 1161, 1162, 1163, 1164, 1165, 1166, 1167, 1168, 1169, 117, 1170, 1171, 1172, 1173, 1174, 1175, 1176, 1177, 1178, 1179, 118, 1180, 1181, 1182, 1183, 1184, 1185, 1186, 1187, 1188, 1189, 119, 1190, 1191, 1192, 1193, 1194, 1195, 1196, 1197, 1198, 1199, 12, 120, 1200, 1201, 1202, 1203, 1204, 1205, 1206, 1207, 1208, 1209, 121, 1210, 1211, 1212, 1213, 1214, 1215, 1216, 1217, 1218, 1219, 122, 1220, 1221, 1222, 1223, 1224, 1225, 1226, 1227, 1228, 1229, 123, 1230, 1231, 1232, 1233, 1234, 1235, 1236, 1237, 1238, 1239, 124, 1240, 1241, 1242, 1243, 1244, 1245, 1246, 1247, 1248, 1249, 125, 1250, 1251, 1252, 1253, 1254, 1255, 1256, 1257, 1258, 1259, 126, 1260, 1261, 1262, 1263, 1264, 1265, 1266, 1267, 1268, 1269, 127, 1270, 1271, 1272, 1273, 1274, 1275, 1276, 1277, 1278, 1279, 128, 1280, 1281, 1282, 1283, 1284, 1285, 1286, 1287, 1288, 1289, 129, 1290, 1291, 1292, 1293, 1294, 1295, 13, 130, 131, 132, 133, 134, 135, 136, 137, 138, 139, 14, 140, 141, 142, 143, 144, 145, 146, 147, 148, 149, 15, 150, 151, 152, 153, 154, 155, 156, 157, 158, 159, 16, 160, 161, 162, 163, 164, 165, 166, 167, 168, 169, 17, 170, 171, 172, 173, 174, 175, 176, 177, 178, 179, 18, 180, 181, 182, 183, 184, 185, 186, 187, 188, 189, 19, 190, 191, 193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: , 
- added C13: C_Small, Capacitor_THT:CP_Radial_D5.0mm_P2.50mm, F.Cu at (111.8, 134.6)
- added R15: R_US, Resistor_THT:R_Axial_DIN0207_L6.3mm_D2.5mm_P2.54mm_Vertical, F.Cu at (106.7, 132.1)
- added R16: R_US, Resistor_THT:R_Axial_DIN0207_L6.3mm_D2.5mm_P2.54mm_Vertical, F.Cu at (106.7, 137.2)
- C11: value C -> 10u
- R13: value R_US -> 10k
- R14: value R_US -> 3k3
- moved U11 2.54 mm to (111.8, 116.8)
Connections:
- U11 pad 2: +5V -> /Contador BCD UP/POR
- U11 pad 6: +5V -> /Contador BCD UP/POR
- U12 pad 2: +5V -> /Contador BCD UP/POR
- U12 pad 6: +5V -> /Contador BCD UP/POR
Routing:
- net /Contador BCD UP/POR: track 0.00 -> 78.7 mm, vias 0 -> 6
- net GND: track 494.3 -> 514.6 mm
- net /Contador BCD UP/Q_{A}: track 61.1 -> 63.7 mm
- net +5V: track 502.8 -> 505.3 mm
- net Net-(U11B-J): track 43.1 -> 40.6 mm
- net /Contador BCD UP/CLK: track 81.2 -> 78.8 mm, vias 7 -> 8
- net /Contador BCD UP/Q_{B}: track 33.0 -> 30.6 mm
